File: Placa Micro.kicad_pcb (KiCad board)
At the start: 2 copper layers, 82 parts

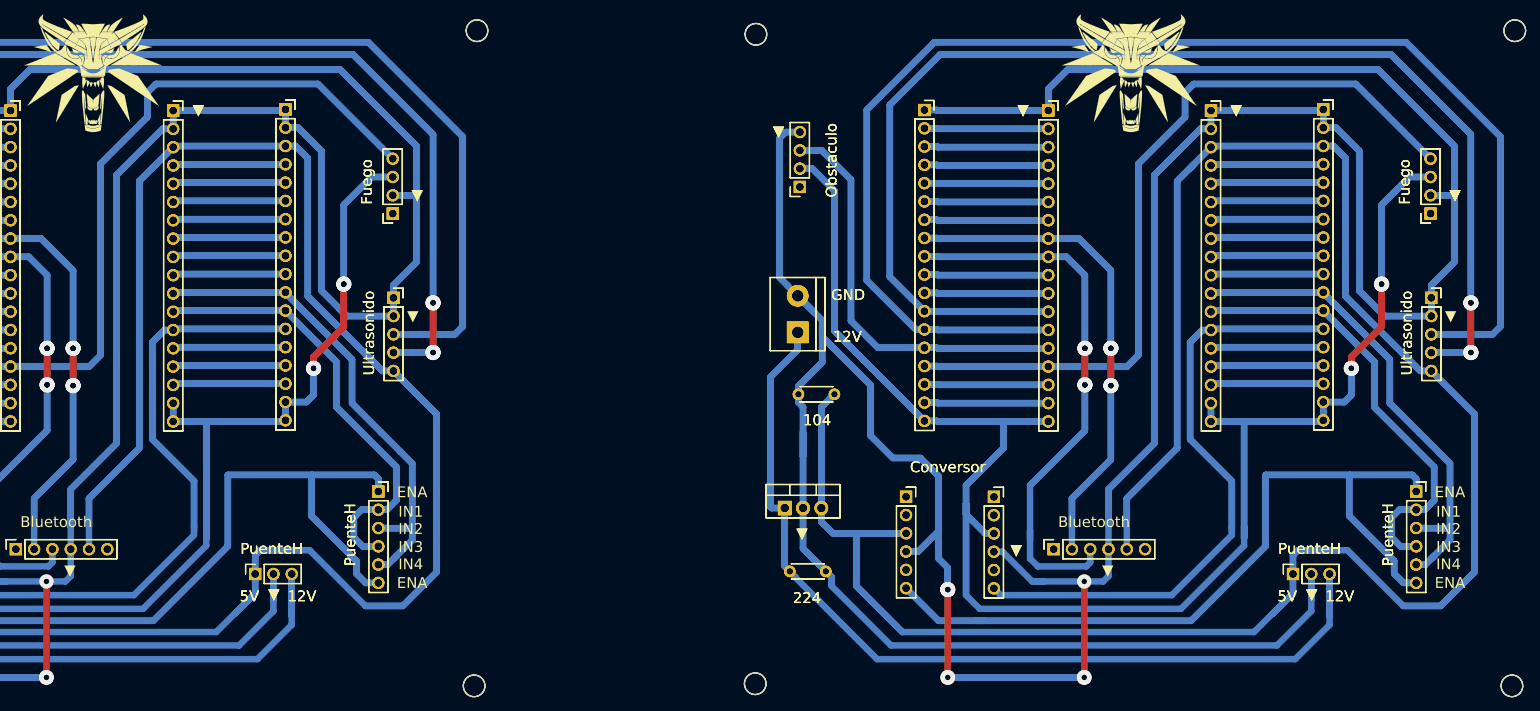
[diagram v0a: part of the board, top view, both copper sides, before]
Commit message: Se agrego GND del Servo
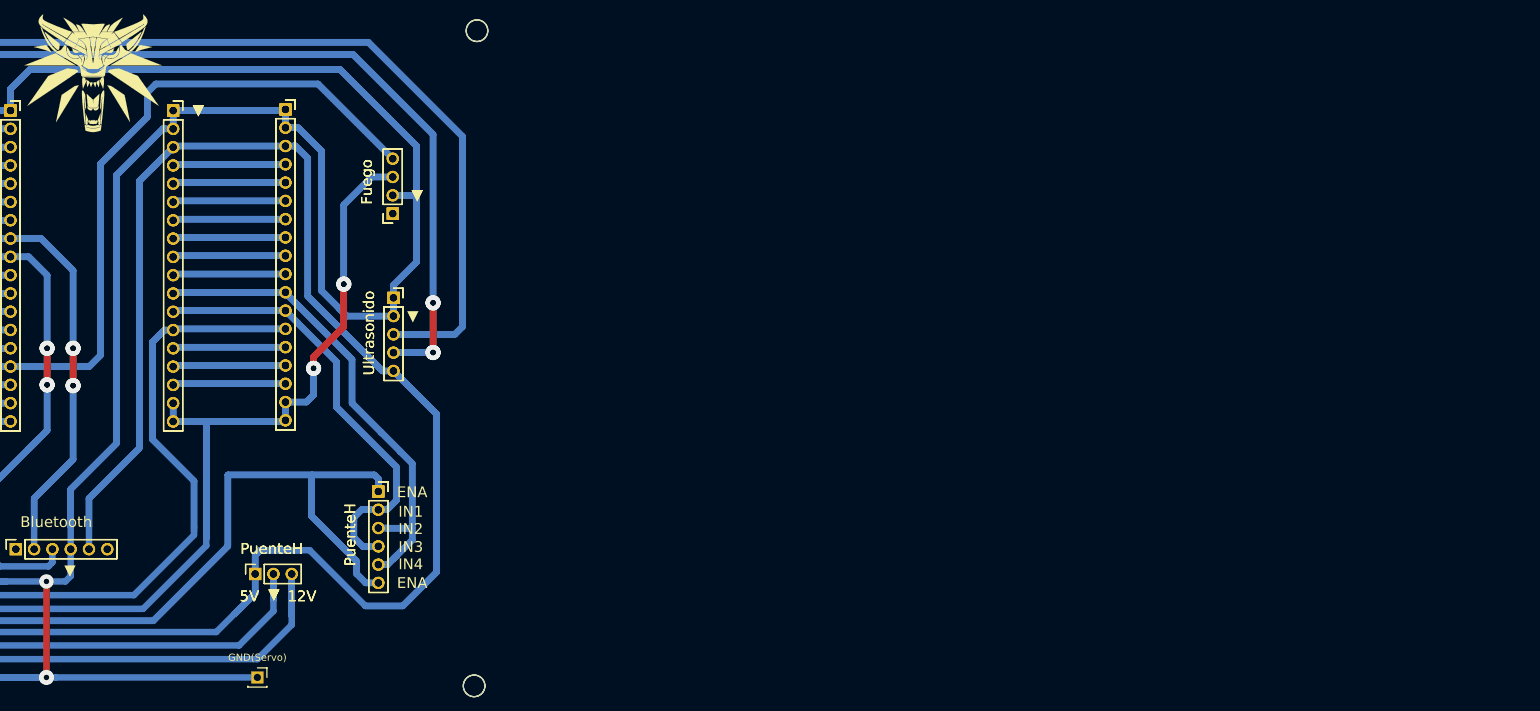
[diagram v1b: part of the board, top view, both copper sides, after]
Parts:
- removed the ? at (222.9, 41.3)
- removed the ? at (264.6, 72.4) (x2)
- removed the ? at (262.5, 99.3) (x2)
- removed the ? at (174.8, 101.6) (x2)
- removed the ? at (234.0, 46.4) (x2)
- removed the ? at (264.5, 60.7) (x2)
- removed the ? at (175.5, 110.4) (x2)
- removed the ? at (275.8, 126.3) (x2)
- removed the ? at (249.6, 46.2) (x2)
- removed the ? at (181.7, 85.8) (x2)
- removed the ? at (203.9, 100.0) (x2)
- removed the ? at (176.9, 57.0) (x2)
- removed the ? at (170.8, 35.8) (x2)
- removed the ? at (194.2, 46.3) (x2)
- removed the ? at (170.7, 126.0) (x2)
- removed the ? at (276.2, 35.3) (x2)
- removed the ? at (245.4, 110.7) (x2)
- removed the ? at (191.7, 100.0) (x2)
- removed the ? at (211.5, 46.4) (x2)
- removed the ? at (176.6, 77.2) (x2)
- removed the ? at (212.2, 107.3) (x2)
- added GND(Servo): Conn_01x01_Female, Connector_PinSocket_2.54mm:PinSocket_1x01_P2.54mm_Vertical, F.Cu at (101.6, 125.1)
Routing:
- net (no net): track 4568.7 -> 0.00 mm, vias 21 -> 0
- net GND: track 903.5 -> 932.8 mm

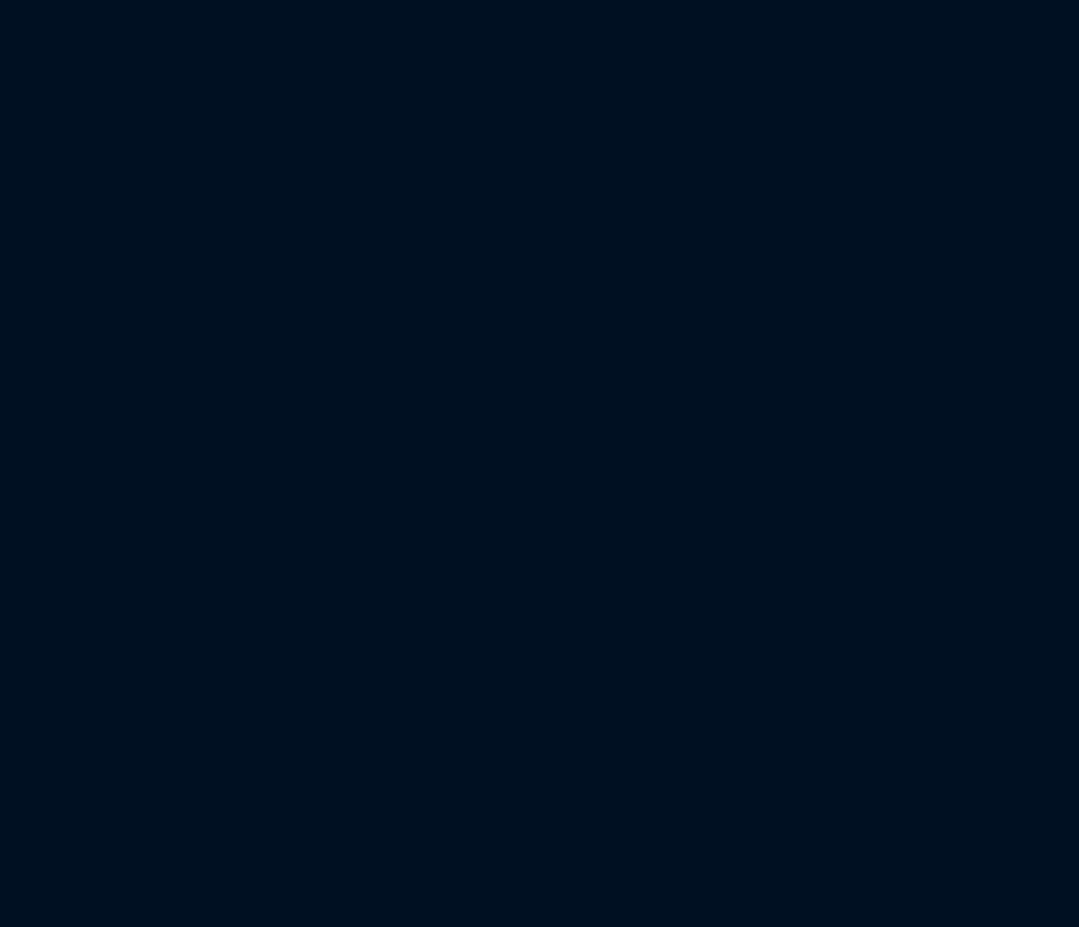
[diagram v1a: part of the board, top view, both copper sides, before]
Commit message: Se actualizaron los PDF
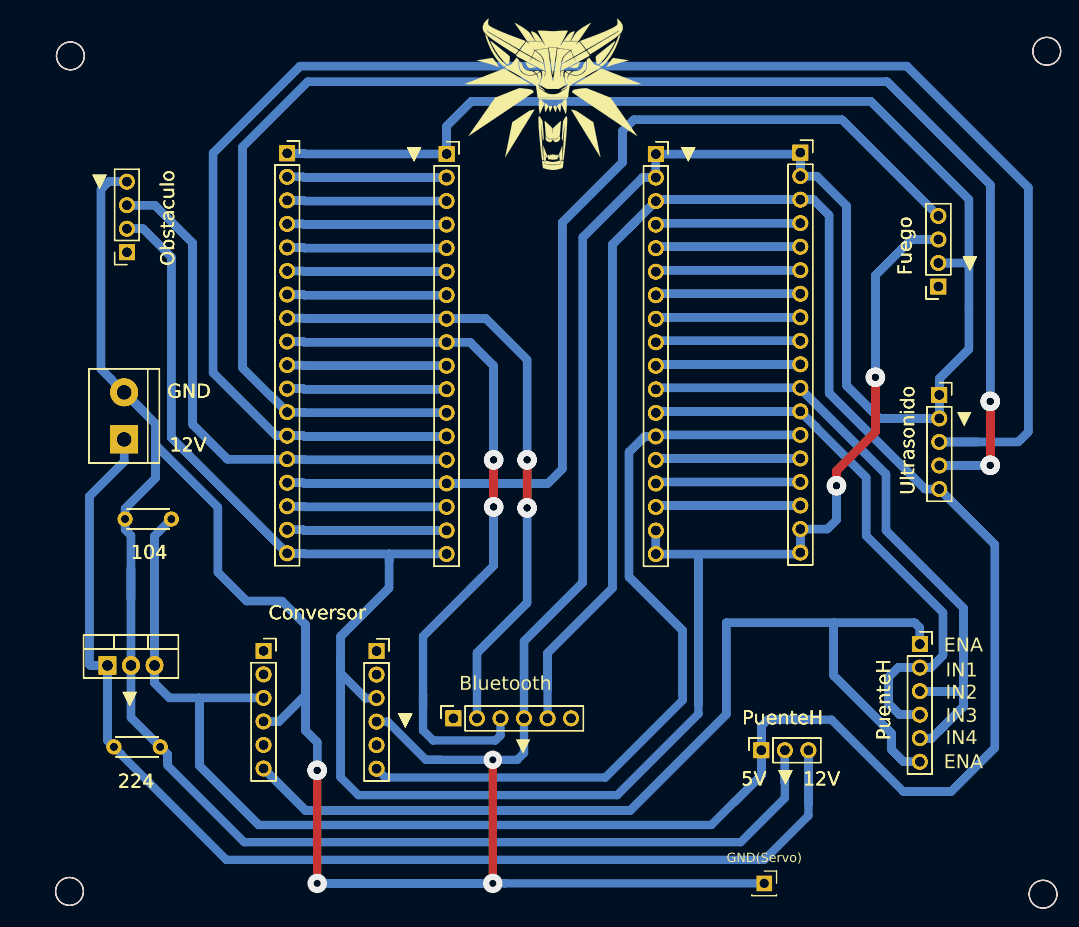
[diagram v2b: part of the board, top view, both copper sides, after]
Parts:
- added ?: , Logos:Witcher_masgrande_sfrontal, F.Cu at (222.2, 40.6)
- added ? (x2): 104, Capacitor_THT:C_Disc_D4.3mm_W1.9mm_P5.00mm, F.Cu at (181.1, 86.4)
- added ? (x2): Conn_01x06_Female, Connector_PinSocket_2.54mm:PinSocket_1x06_P2.54mm_Vertical, F.Cu at (191.1, 100.6)
- added ? (x2): Conn_01x06_Female, Connector_PinSocket_2.54mm:PinSocket_1x06_P2.54mm_Vertical, F.Cu at (203.3, 100.7)
- added ? (x2): Conn_01x05_Female, Connector_PinSocket_2.54mm:PinSocket_1x05_P2.54mm_Vertical, F.Cu at (264.0, 73.0)
- added ? (x2): MountingHole, MountingHole:MountingHole_3mm, F.Cu at (275.2, 126.9)
- added ? (x2): Conn_01x06_Female, Connector_PinSocket_2.54mm:PinSocket_1x06_P2.54mm_Vertical, F.Cu at (261.9, 99.9)
- added ? (x2): Screw_Terminal_01x02, TerminalBlock:TerminalBlock_bornier-2_P5.08mm, F.Cu at (176.0, 77.8)
- added ? (x2): Conn_01x18_Female, Connector_PinSocket_2.54mm:PinSocket_1x18_P2.54mm_Vertical, F.Cu at (233.4, 47.0)
- added ? (x2): 224, Capacitor_THT:C_Disc_D4.3mm_W1.9mm_P5.00mm, F.Cu at (174.9, 111.0)
- added ? (x2): MountingHole, MountingHole:MountingHole_3mm, F.Cu at (170.1, 126.6)
- added ? (x2): MountingHole, MountingHole:MountingHole_3mm, F.Cu at (170.2, 36.4)
- added ? (x2): Conn_01x03_Female, Connector_PinSocket_2.54mm:PinSocket_1x03_P2.54mm_Vertical, F.Cu at (244.8, 111.4)
- added ? (x2): Conn_01x04_Female, Connector_PinSocket_2.54mm:PinSocket_1x04_P2.54mm_Vertical, F.Cu at (176.3, 57.6)
- added ? (x2): MountingHole, MountingHole:MountingHole_3mm, F.Cu at (275.6, 35.9)
- added ? (x2): Conn_01x18_Female, Connector_PinSocket_2.54mm:PinSocket_1x18_P2.54mm_Vertical, F.Cu at (249.0, 46.8)
- added ? (x2): L7805, Package_TO_SOT_THT:TO-220-3_Vertical, F.Cu at (174.2, 102.2)
- added ? (x2): Conn_01x18_Female, Connector_PinSocket_2.54mm:PinSocket_1x18_P2.54mm_Vertical, F.Cu at (193.6, 46.9)
- added ? (x2): Conn_01x18_Female, Connector_PinSocket_2.54mm:PinSocket_1x18_P2.54mm_Vertical, F.Cu at (210.8, 47.0)
- added ? (x2): Conn_01x04_Female, Connector_PinSocket_2.54mm:PinSocket_1x04_P2.54mm_Vertical, F.Cu at (263.9, 61.3)
- added ? (x2): Conn_01x06_Female, Connector_PinSocket_2.54mm:PinSocket_1x06_P2.54mm_Vertical, F.Cu at (211.6, 107.9)
- added GND(Servo): Conn_01x01_Female, Connector_PinSocket_2.54mm:PinSocket_1x01_P2.54mm_Vertical, F.Cu at (245.1, 125.7)
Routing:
- net (no net): track 0.00 -> 4598.0 mm, vias 0 -> 21
